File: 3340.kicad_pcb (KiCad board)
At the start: 2 copper layers, 50.8 x 106.7 mm, 181 parts, among them J1 Conn_01x16, J10 FM1, J11 Conn_01x16, J12 V/OCT2, J13 PULSE2, J14 SAW2, J15 TRI2, J16 SINE2, J17 SYNC2, J18 Conn_01x16, J19 PWM2, J2 Conn_01x16, J20 FM2, J3 V/OCT1, J4 PULSE1, J5 SAW1, J6 TRI1, J7 SINE1, J8 SYNC1, J9 PWM1, Q1 2N3904, Q2 2N3906, Q3 2N3904, Q4 2N3906, Q5 2N3904, Q6 2N3904, SW2 DPDT_OOO, U1 TL072, U2 TL074, U3 CEM3340, U4 TL072, U5 CEM3340, U6 TL074

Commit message: Fix power routing
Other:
- board size 50.8 x 106.7 mm -> 110.5 x 106.7 mm
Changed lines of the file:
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@@
   (gr_rect (start -110.49 31.75) (end -99.06 138.43) (layer "F.SilkS") (width 0.15) (fill none))
   (gr_rect (start 12.7 12.7) (end 63.5 119.38) (layer "Edge.Cuts") (width 0.1) (fill none))
+  (gr_rect (start 63.5 12.7) (end 123.19 119.38) (layer "Edge.Cuts") (width 0.1) (fill none))
   (segment (start 49.28601 50.8) (end 46.99 50.8) (width 0.25) (layer "B.Cu") (net 1))
   (segment (start 41.99 43.825) (end 45.155 46.99) (width 0.25) (layer "B.Cu") (net 1))

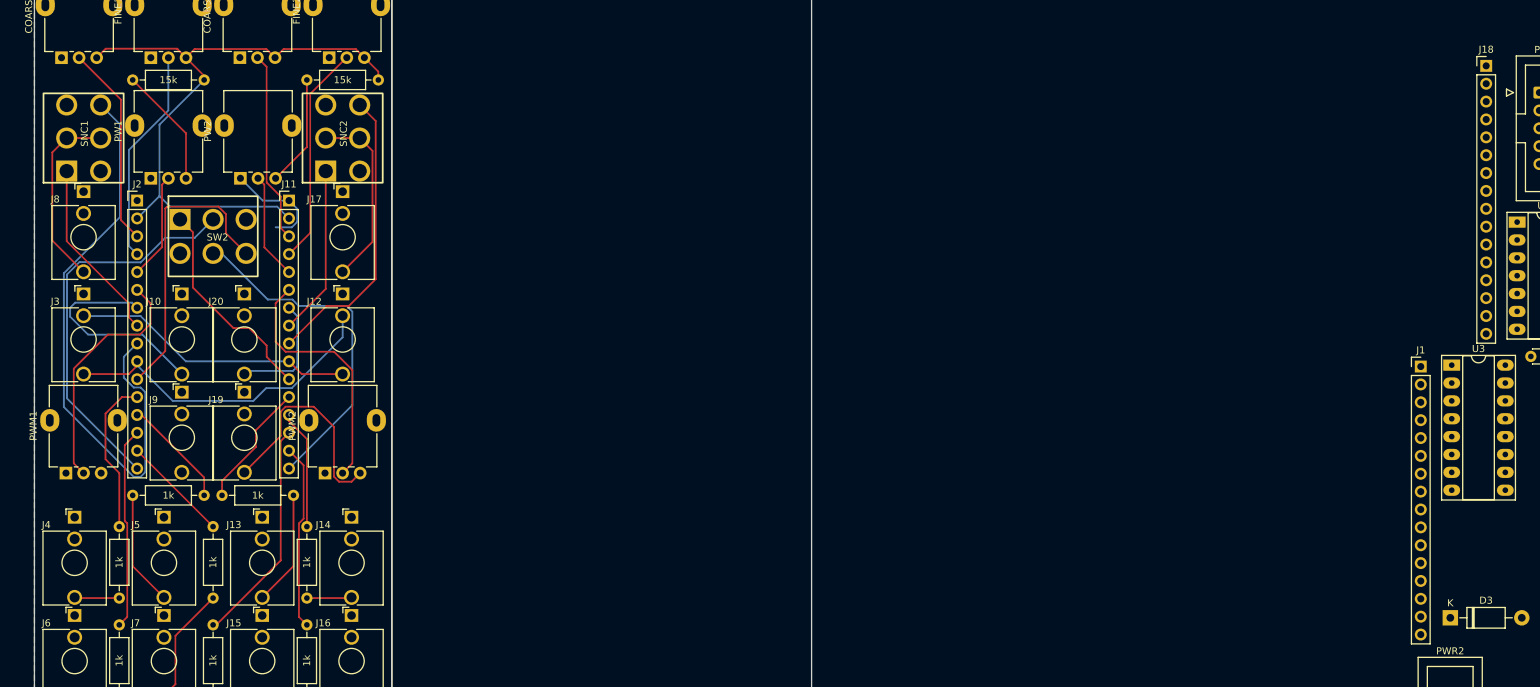
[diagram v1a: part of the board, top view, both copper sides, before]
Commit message: Update pin header footprints
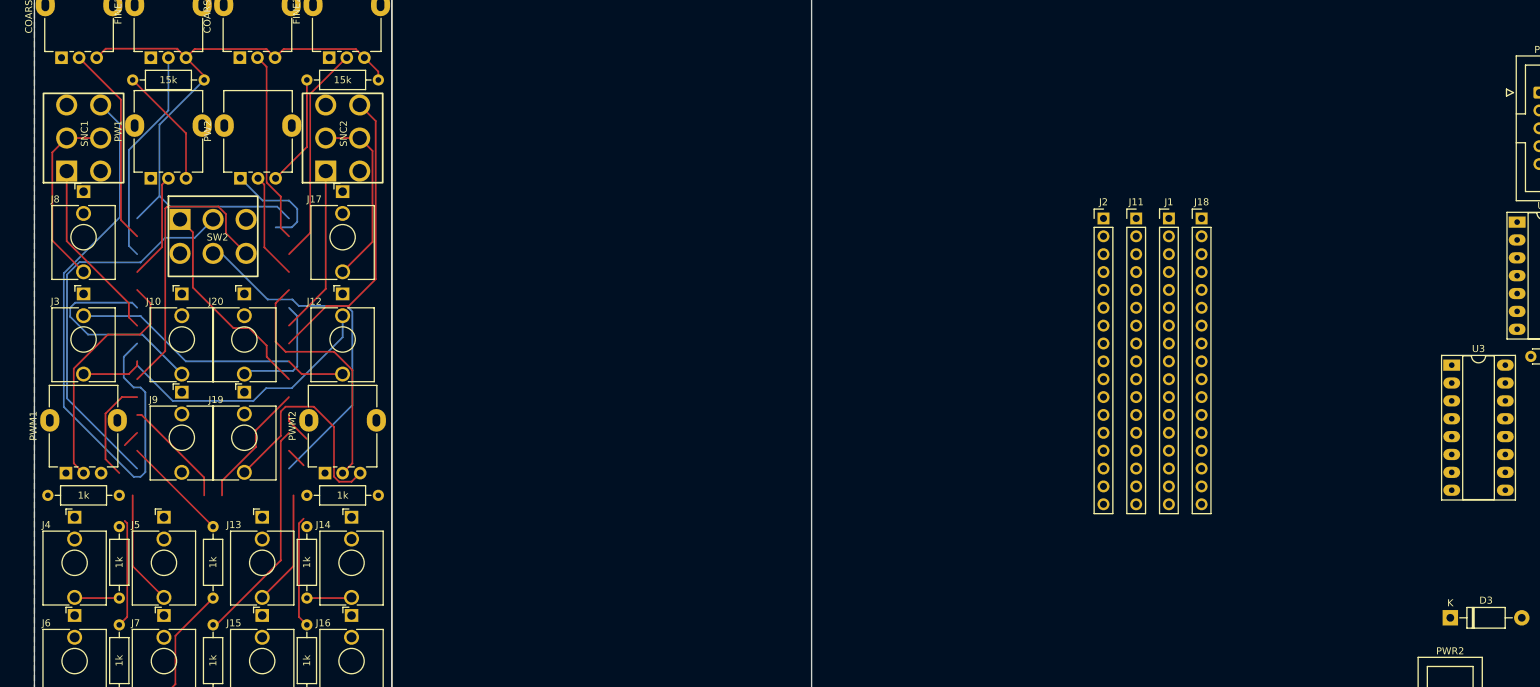
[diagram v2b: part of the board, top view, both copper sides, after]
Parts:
- J1, J11, J18, J2: value Conn_01x16 -> Conn_01x17; footprint Connector_PinHeader_2.54mm:PinHeader_1x16_P2.54mm_Vertical -> Connector_PinHeader_2.54mm:PinHeader_1x17_P2.54mm_Vertical
- moved J2 137.4 mm to (164.7, 49.5)
- moved J11 120.5 mm to (169.3, 49.5)
- moved J18 45.9 mm to (178.6, 49.5)
- moved J1 41.5 mm to (174.0, 49.5)
- moved R73 12.1 mm to (51.4, 88.9)
- moved R37 12.1 mm to (24.8, 88.9)
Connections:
- J1 pad 1: GND -> -12V
- J1 pad 10: /V/OCT1 -> /SYNC-1
- J1 pad 11: /SAWIN1 -> /V/OCT1
- J1 pad 12: /PULSEOUT1 -> /SAWIN1
- J1 pad 13: /SAWOUT1 -> /PULSEOUT1
- J1 pad 14: /SHAPE1 -> /SAWOUT1
- J1 pad 15: /SINE1 -> /SHAPE1
- J1 pad 16: /SAW1 -> /SINE1
- J1 pad 2: +12V -> GND
- J1 pad 3: /COARSE1 -> +12V
- J1 pad 4: /FINE1 -> /COARSE1
- J1 pad 5: /PW_IN1 -> /FINE1
- J1 pad 6: /PWM_IN1 -> /PW_IN1
- J1 pad 7: /FMOD1 -> /PWM_IN1
- J1 pad 8: /SYNC+1 -> /FMOD1
- J1 pad 9: /SYNC-1 -> /SYNC+1
- J11 pad 1: GND -> /-12
- J11 pad 10: /VOCT2 -> Net-(SNC2-Pad6)
- J11 pad 11: /SAW_IN2 -> /VOCT2
- J11 pad 12: Net-(J11-Pad12) -> /SAW_IN2
- J11 pad 13: Net-(J11-Pad13) -> Net-(R73-Pad1)
- J11 pad 14: Net-(J11-Pad14) -> Net-(R74-Pad1)
- J11 pad 15: Net-(J11-Pad15) -> Net-(R75-Pad1)
- J11 pad 16: /SAW21 -> Net-(R76-Pad1)
- J11 pad 2: /12v -> GND
- J11 pad 3: Net-(COARSE2-Pad2) -> /12v
- J11 pad 4: Net-(FINE2-Pad2) -> Net-(COARSE2-Pad2)
- J11 pad 5: Net-(J11-Pad5) -> Net-(FINE2-Pad2)
- J11 pad 6: Net-(J11-Pad6) -> Net-(PW2-Pad2)
- J11 pad 7: Net-(J11-Pad7) -> Net-(PWM2-Pad2)
- J11 pad 8: Net-(J11-Pad8) -> Net-(J20-PadT)
- J11 pad 9: Net-(J11-Pad9) -> Net-(SNC2-Pad1)
- J18 pad 1: GND -> -12V
- J18 pad 10: /V/OCT2 -> /SYNC-2
- J18 pad 11: /SAWIN2 -> /V/OCT2
- J18 pad 12: /PULSEOUT2 -> /SAWIN2
- J18 pad 13: /SAWOUT2 -> /PULSEOUT2
- J18 pad 14: /SHAPE2 -> /SAWOUT2
- J18 pad 15: /SINE2 -> /SHAPE2
- J18 pad 16: /SAW2 -> /SINE2
- J18 pad 2: +12V -> GND
- J18 pad 3: /COARSE2 -> +12V
- J18 pad 4: /FINE2 -> /COARSE2
- J18 pad 5: /PW_IN2 -> /FINE2
- J18 pad 6: /PWM_IN2 -> /PW_IN2
- J18 pad 7: /FMOD2 -> /PWM_IN2
- J18 pad 8: /SYNC+2 -> /FMOD2
- J18 pad 9: /SYNC-2 -> /SYNC+2
- J2 pad 1: GND -> /-12
- J2 pad 10: /VOCT1 -> Net-(SNC1-Pad6)
- J2 pad 11: /SAW_IN1 -> /VOCT1
- J2 pad 12: Net-(J2-Pad12) -> /SAW_IN1
- J2 pad 13: Net-(J2-Pad13) -> Net-(R36-Pad1)
- J2 pad 14: Net-(J2-Pad14) -> Net-(R37-Pad1)
- J2 pad 15: Net-(J2-Pad15) -> Net-(R38-Pad1)
- J2 pad 16: /SAW12 -> Net-(R39-Pad1)
- J2 pad 2: /12v -> GND
- J2 pad 3: Net-(COARSE1-Pad2) -> /12v
- J2 pad 4: Net-(FINE1-Pad2) -> Net-(COARSE1-Pad2)
- J2 pad 5: Net-(J2-Pad5) -> Net-(FINE1-Pad2)
- J2 pad 6: Net-(J2-Pad6) -> Net-(PW1-Pad2)
- J2 pad 7: Net-(J10-PadT) -> Net-(PWM1-Pad2)
- J2 pad 8: Net-(J2-Pad8) -> Net-(J10-PadT)
- J2 pad 9: Net-(J2-Pad9) -> Net-(SNC1-Pad1)
- J20 pad T: Net-(J11-Pad7) -> Net-(J20-PadT)
- PW1 pad 2: Net-(J2-Pad5) -> Net-(PW1-Pad2)
- PW2 pad 2: Net-(J11-Pad5) -> Net-(PW2-Pad2)
- PWM1 pad 2: Net-(J2-Pad6) -> Net-(PWM1-Pad2)
- PWM2 pad 2: Net-(J11-Pad6) -> Net-(PWM2-Pad2)
- R36 pad 1: Net-(J2-Pad12) -> Net-(R36-Pad1)
- R37 pad 1: Net-(J2-Pad13) -> Net-(R37-Pad1)
- R38 pad 1: Net-(J2-Pad14) -> Net-(R38-Pad1)
- R39 pad 1: Net-(J2-Pad15) -> Net-(R39-Pad1)
- R73 pad 1: Net-(J11-Pad12) -> Net-(R73-Pad1)
- R74 pad 1: Net-(J11-Pad13) -> Net-(R74-Pad1)
- R75 pad 1: Net-(J11-Pad14) -> Net-(R75-Pad1)
- R76 pad 1: Net-(J11-Pad15) -> Net-(R76-Pad1)
- SNC1 pad 1: Net-(J2-Pad8) -> Net-(SNC1-Pad1)
- SNC1 pad 6: Net-(J2-Pad9) -> Net-(SNC1-Pad6)
- SNC2 pad 1: Net-(J11-Pad8) -> Net-(SNC2-Pad1)
- SNC2 pad 6: Net-(J11-Pad9) -> Net-(SNC2-Pad6)
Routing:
- net Net-(SNC1-Pad6): track 0.00 -> 84.3 mm
- net Net-(J2-Pad9): track 84.3 -> 0.00 mm
- net Net-(SNC2-Pad6): track 0.00 -> 41.8 mm
- net Net-(J11-Pad9): track 41.8 -> 0.00 mm
- net Net-(PWM2-Pad2): track 0.00 -> 36.0 mm
- net Net-(J11-Pad6): track 36.0 -> 0.00 mm
- net Net-(PWM1-Pad2): track 0.00 -> 34.6 mm
- net Net-(J2-Pad6): track 34.6 -> 0.00 mm
- net Net-(R75-Pad1): track 0.00 -> 32.0 mm
- net Net-(J11-Pad14): track 32.0 -> 0.00 mm
- net Net-(J2-Pad14): track 28.6 -> 0.00 mm
- net Net-(J11-Pad15): track 26.4 -> 0.00 mm
- net Net-(SNC1-Pad1): track 0.00 -> 26.1 mm
- net Net-(J2-Pad8): track 26.1 -> 0.00 mm
- net Net-(SNC2-Pad1): track 0.00 -> 24.1 mm
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
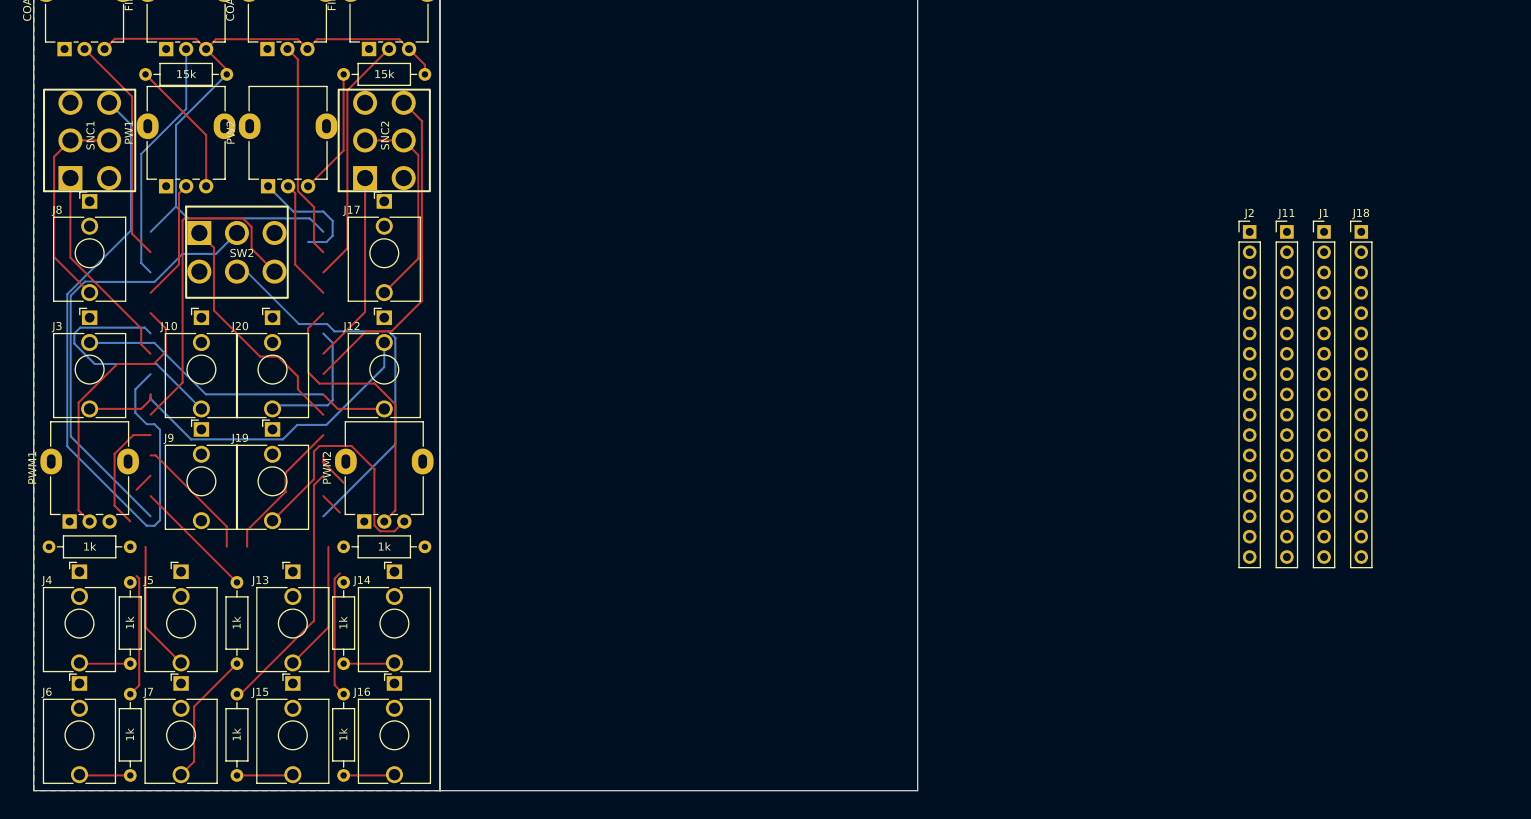
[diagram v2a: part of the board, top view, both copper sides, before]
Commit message: Fix synch switches in schematic
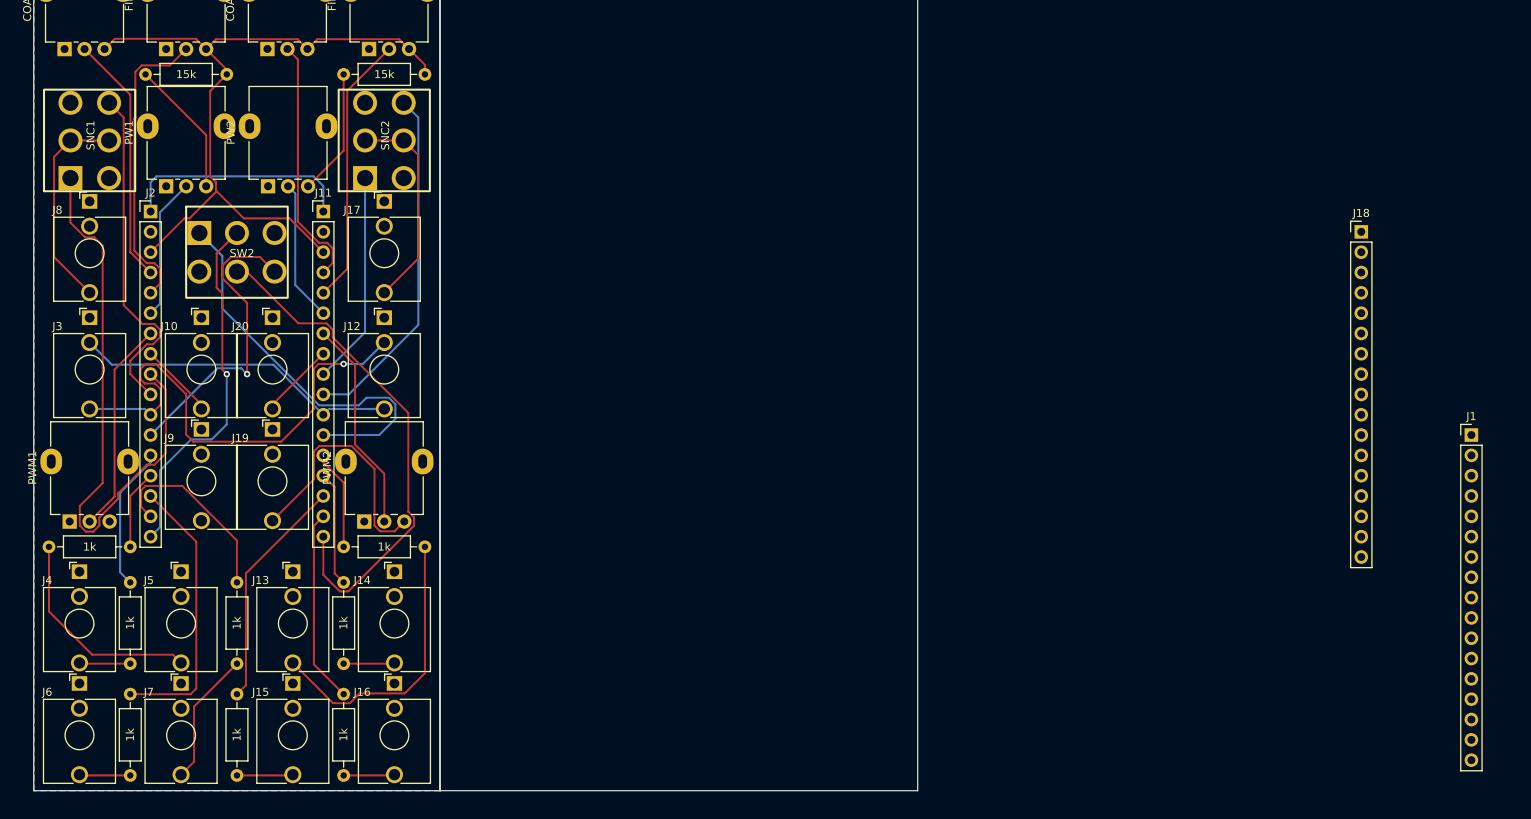
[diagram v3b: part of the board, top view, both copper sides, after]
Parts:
- moved J2 137.4 mm to (27.3, 47.0)
- moved J11 120.5 mm to (48.9, 47.0)
- moved J1 31.4 mm to (192.4, 74.9)
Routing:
- net Net-(SNC1-Pad1): track 26.1 -> 73.8 mm
- net Net-(SNC1-Pad6): track 84.3 -> 43.0 mm
- net /-12: track 0.00 -> 29.2 mm
- net Net-(J10-PadT): track 30.7 -> 9.53 mm
- net Net-(J13-PadT): track 16.4 -> 35.9 mm
- net /SAW_IN2: track 30.4 -> 49.7 mm
- net Net-(R38-Pad1): track 17.9 -> 35.0 mm
- net GND: track 15.1 -> 0.00 mm
- net /SAW21: track 49.3 -> 64.1 mm
- net /VOCT1: track 47.4 -> 61.7 mm, vias 0 -> 1
- net Net-(J5-PadT): track 16.4 -> 27.3 mm
- net /SAW12: track 55.8 -> 45.0 mm, vias 0 -> 1
- net Net-(R74-Pad1): track 4.47 -> 14.4 mm
- net Net-(PWM2-Pad2): track 36.0 -> 26.7 mm
- net Net-(R39-Pad1): track 15.3 -> 24.0 mm
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
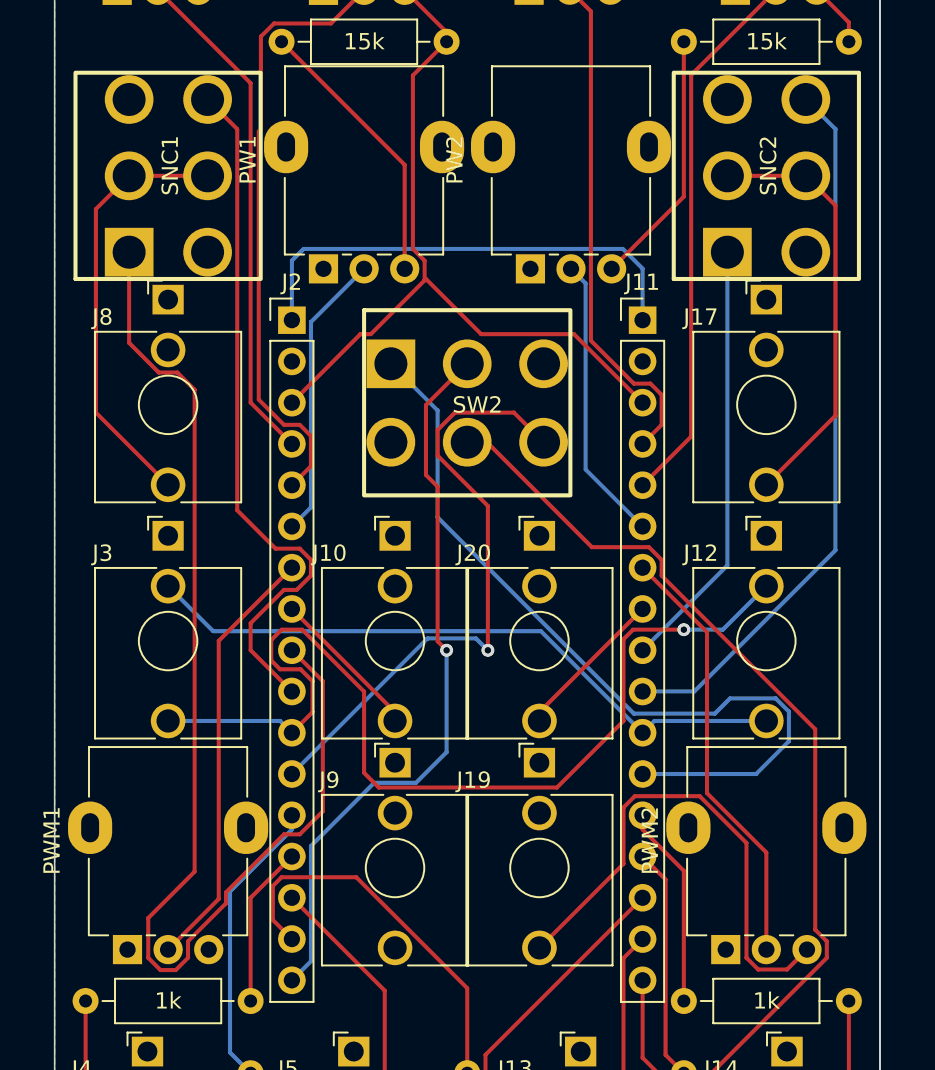
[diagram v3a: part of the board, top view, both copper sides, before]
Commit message: Fix sync switches on board
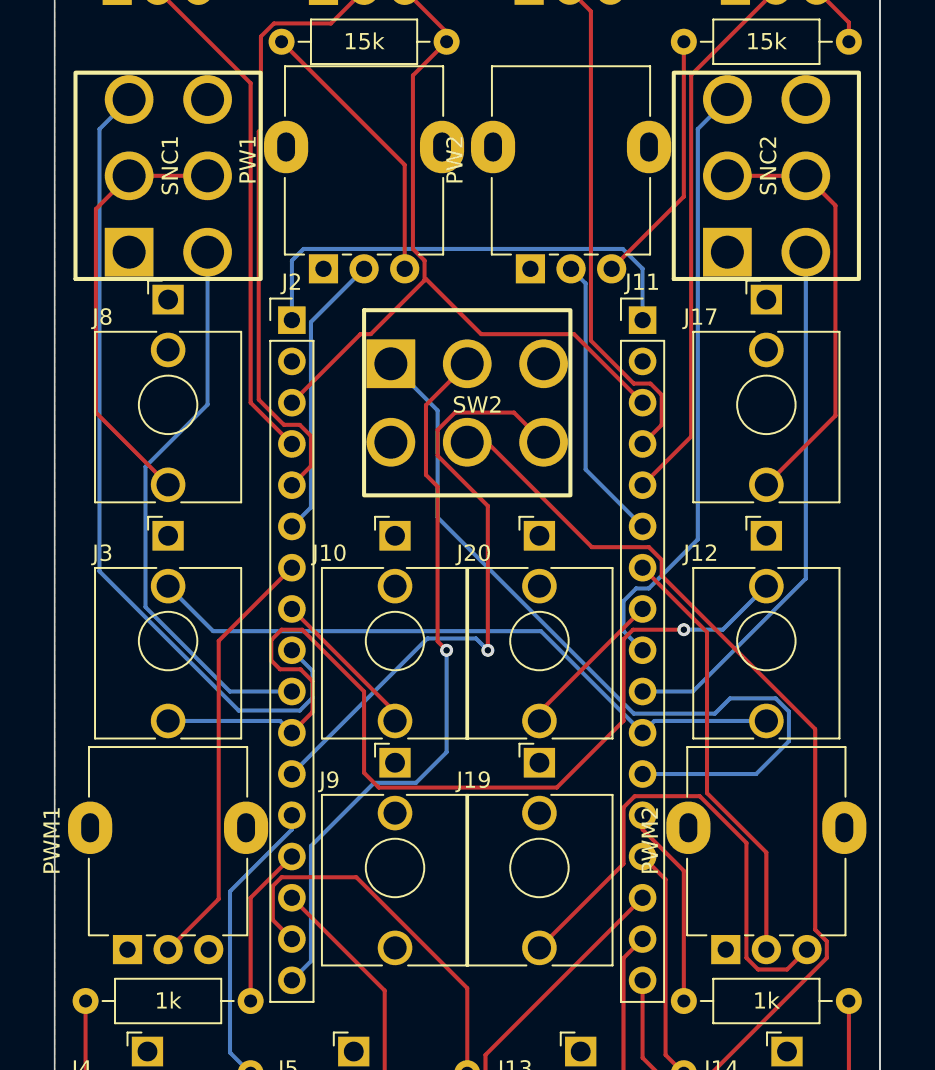
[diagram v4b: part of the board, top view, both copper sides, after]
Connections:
- J11 pad 10: Net-(SNC2-Pad6) -> Net-(J11-Pad10)
- J11 pad 9: Net-(SNC2-Pad1) -> Net-(J11-Pad9)
- J2 pad 10: Net-(SNC1-Pad6) -> Net-(J2-Pad10)
- J2 pad 9: Net-(SNC1-Pad1) -> Net-(J2-Pad9)
- SNC1 pad 1: Net-(SNC1-Pad1) -> unconnected-(SNC1-Pad1)
- SNC1 pad 3: unconnected-(SNC1-Pad3) -> Net-(J2-Pad9)
- SNC1 pad 4: unconnected-(SNC1-Pad4) -> Net-(J2-Pad10)
- SNC1 pad 6: Net-(SNC1-Pad6) -> unconnected-(SNC1-Pad6)
- SNC2 pad 1: Net-(SNC2-Pad1) -> unconnected-(SNC2-Pad1)
- SNC2 pad 3: unconnected-(SNC2-Pad3) -> Net-(J11-Pad9)
- SNC2 pad 4: unconnected-(SNC2-Pad4) -> Net-(J11-Pad10)
- SNC2 pad 6: Net-(SNC2-Pad6) -> unconnected-(SNC2-Pad6)
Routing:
- net Net-(SNC1-Pad1): track 73.8 -> 0.00 mm
- net Net-(J2-Pad9): track 0.00 -> 50.3 mm
- net Net-(SNC2-Pad6): track 44.0 -> 0.00 mm
- net Net-(SNC1-Pad6): track 43.0 -> 0.00 mm
- net Net-(J11-Pad9): track 0.00 -> 37.5 mm
- net Net-(J2-Pad10): track 0.00 -> 34.6 mm
- net Net-(J11-Pad10): track 0.00 -> 33.0 mm
- net Net-(SNC2-Pad1): track 26.7 -> 0.00 mm
